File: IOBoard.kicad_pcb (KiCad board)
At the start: 2 copper layers, 119.8 x 63.7 mm, 29 parts, among them J12 DE9_Receptacle, J13 DE9_Plug, J14 DE9_Receptacle, J15 DE9_Receptacle, J16 DE9_Receptacle, J3 Conn_01x03, J4 Conn_01x03, J5 Conn_01x03, J6 Conn_01x03, J7 Conn_01x03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

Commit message: Update schematic and PCB to use resistor symbols instead of jumpers.
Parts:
- removed JP1, JP10, JP11, JP12, JP13, JP14, JP15, JP16, JP2, JP3, JP4, JP5, JP6, JP7, JP8, JP9: Jumper_2_Open, Resistor_THT:R_Axial_DIN0207_L6.3mm_D2.5mm_P10.16mm_Horizontal
- added R10: 120R, Resistor_THT:R_Axial_DIN0207_L6.3mm_D2.5mm_P7.62mm_Horizontal, F.Cu at (156.2, 121.9)
- added R11: 120R, Resistor_THT:R_Axial_DIN0207_L6.3mm_D2.5mm_P7.62mm_Horizontal, F.Cu at (156.2, 118.1)
- added R12: 120R, Resistor_THT:R_Axial_DIN0207_L6.3mm_D2.5mm_P7.62mm_Horizontal, F.Cu at (156.2, 114.3)
- added R13: 120R, Resistor_THT:R_Axial_DIN0207_L6.3mm_D2.5mm_P7.62mm_Horizontal, F.Cu at (156.2, 110.5)
- added R14: 120R, Resistor_THT:R_Axial_DIN0207_L6.3mm_D2.5mm_P7.62mm_Horizontal, F.Cu at (156.2, 106.7)
- added R15: 120R, Resistor_THT:R_Axial_DIN0207_L6.3mm_D2.5mm_P7.62mm_Horizontal, F.Cu at (156.2, 102.9)
- added R16: 120R, Resistor_THT:R_Axial_DIN0207_L6.3mm_D2.5mm_P7.62mm_Horizontal, F.Cu at (156.2, 99.1)
- added R17: 120R, Resistor_THT:R_Axial_DIN0207_L6.3mm_D2.5mm_P7.62mm_Horizontal, F.Cu at (156.2, 95.2)
- added R2: 120R, Resistor_THT:R_Axial_DIN0207_L6.3mm_D2.5mm_P7.62mm_Horizontal, F.Cu at (125.7, 95.2)
- added R3: 120R, Resistor_THT:R_Axial_DIN0207_L6.3mm_D2.5mm_P7.62mm_Horizontal, F.Cu at (125.7, 99.1)
- added R4: 120R, Resistor_THT:R_Axial_DIN0207_L6.3mm_D2.5mm_P7.62mm_Horizontal, F.Cu at (125.7, 102.9)
- added R5: 120R, Resistor_THT:R_Axial_DIN0207_L6.3mm_D2.5mm_P7.62mm_Horizontal, F.Cu at (125.7, 106.7)
- added R6: 120R, Resistor_THT:R_Axial_DIN0207_L6.3mm_D2.5mm_P7.62mm_Horizontal, F.Cu at (125.7, 110.5)
- added R7: 120R, Resistor_THT:R_Axial_DIN0207_L6.3mm_D2.5mm_P7.62mm_Horizontal, F.Cu at (125.7, 114.3)
- added R8: 120R, Resistor_THT:R_Axial_DIN0207_L6.3mm_D2.5mm_P7.62mm_Horizontal, F.Cu at (125.7, 118.1)
- added R9: 120R, Resistor_THT:R_Axial_DIN0207_L6.3mm_D2.5mm_P7.62mm_Horizontal, F.Cu at (125.7, 121.9)
- moved J16 2.54 mm to (166.4, 113.0)
- moved J15 1.69 mm to (114.4, 102.1)
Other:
- board size 119.8 x 63.7 mm -> 118.5 x 63.7 mm

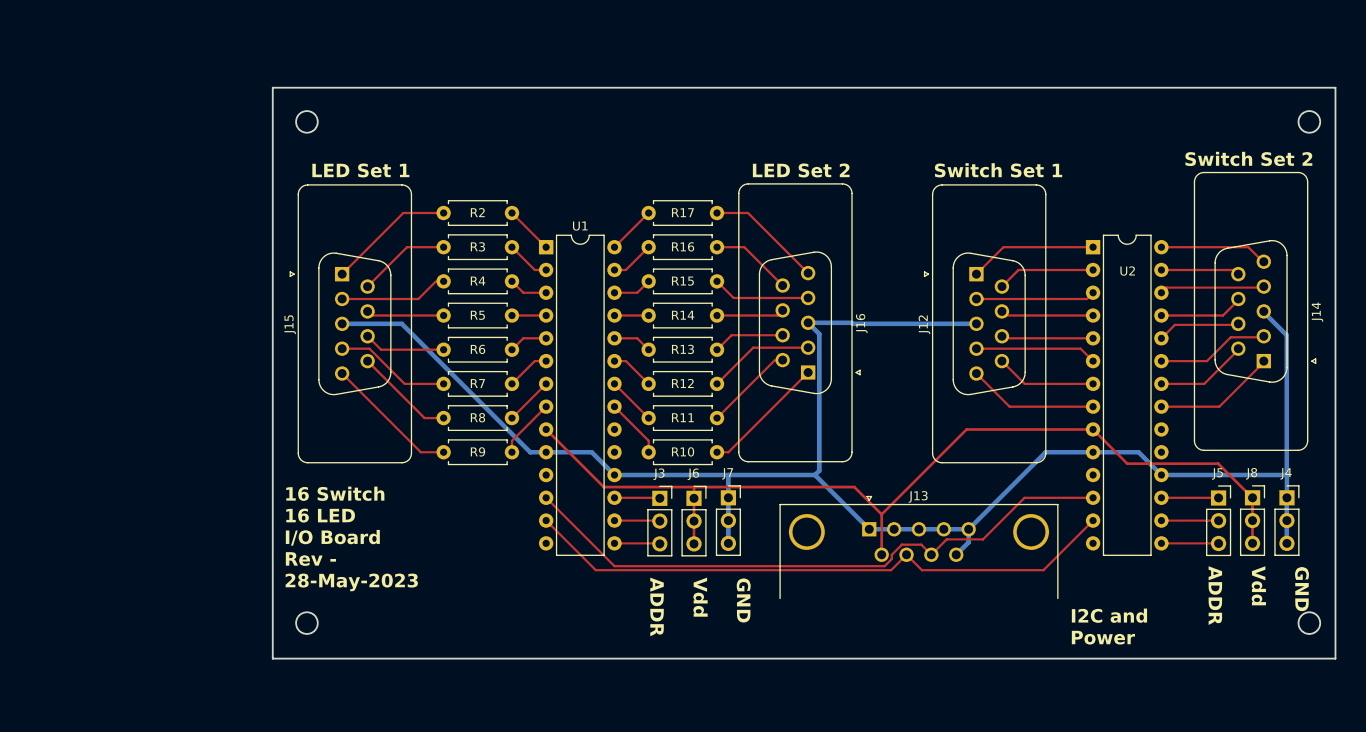
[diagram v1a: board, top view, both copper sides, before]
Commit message: Update PCB to use SMD resistors and rectangular connectors.  This lets the PCB shrink some more and it may be easier to crimp rectangular connectors onto ribbon cable than to solder a bunch of D-9 connectors.
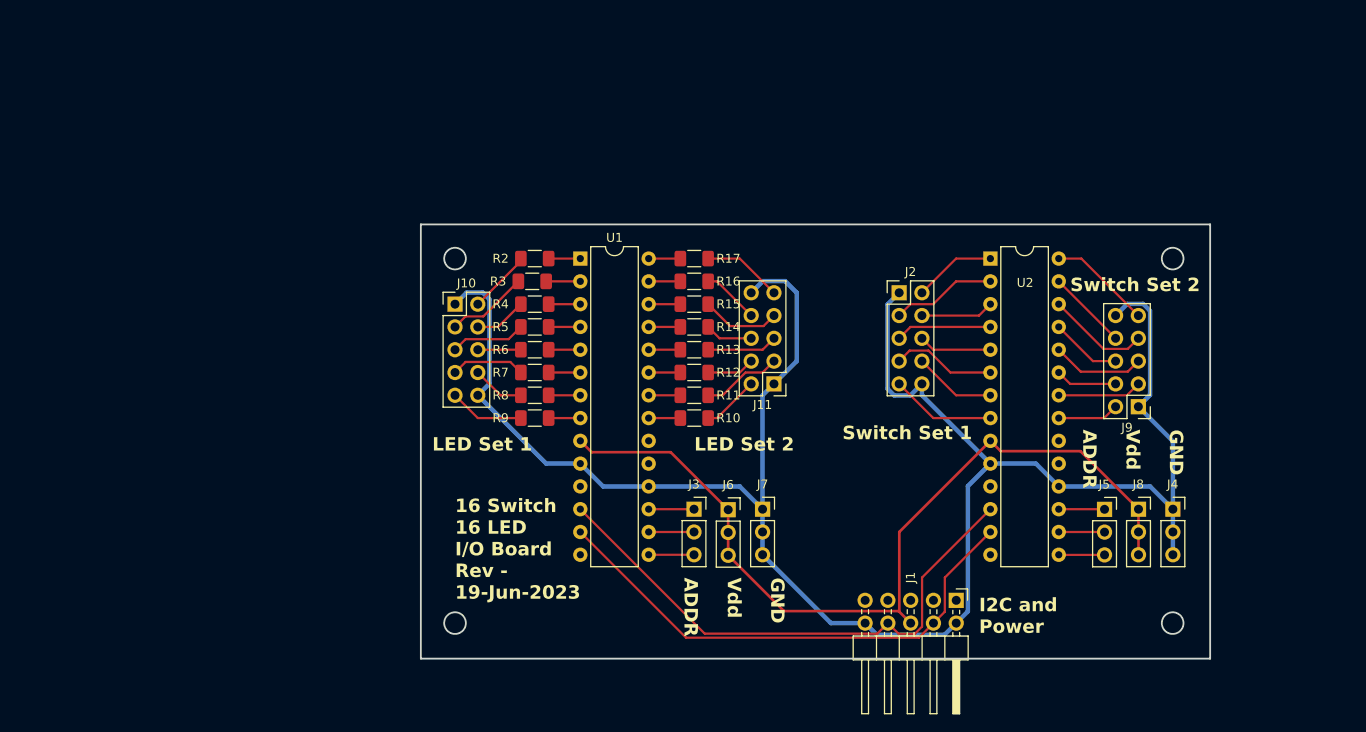
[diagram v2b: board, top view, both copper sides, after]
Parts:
- removed J12, J14, J15, J16: DE9_Receptacle, Connector_Dsub:DSUB-9_Female_Vertical_P2.77x2.84mm
- removed J13: DE9_Plug, Connector_Dsub:DSUB-9_Male_Horizontal_P2.77x2.84mm_EdgePinOffset4.94mm_Housed_MountingHolesOffset7.48mm
- added J1: Conn_02x05_Odd_Even, Connector_PinHeader_2.54mm:PinHeader_2x05_P2.54mm_Horizontal, F.Cu at (182.9, 138.4)
- added J10: Conn_02x05_Odd_Even, Connector_PinHeader_2.54mm:PinHeader_2x05_P2.54mm_Vertical, F.Cu at (127.0, 105.4)
- added J11: Conn_02x05_Odd_Even, Connector_PinHeader_2.54mm:PinHeader_2x05_P2.54mm_Vertical, F.Cu at (162.6, 114.3)
- added J2: Conn_02x05_Odd_Even, Connector_PinHeader_2.54mm:PinHeader_2x05_P2.54mm_Vertical, F.Cu at (176.5, 104.1)
- added J9: Conn_02x05_Odd_Even, Connector_PinHeader_2.54mm:PinHeader_2x05_P2.54mm_Vertical, F.Cu at (203.2, 116.8)
- R10, R11, R12, R13, R14, R15, R16, R17, R2, R3, R4, R5, R6, R7, R8, R9: footprint Resistor_THT:R_Axial_DIN0207_L6.3mm_D2.5mm_P7.62mm_Horizontal -> Resistor_SMD:R_1206_3216Metric_Pad1.30x1.75mm_HandSolder
- moved J4 12.8 mm to (207.0, 128.3)
- moved J8 12.8 mm to (203.2, 128.3)
- moved J5 12.8 mm to (199.4, 128.3)
- moved U2 11.5 mm to (186.7, 100.3)
- moved R2 11.4 mm to (135.9, 100.3)
- moved R9 10.9 mm to (135.9, 118.1)
- moved R3 10.6 mm to (135.6, 102.9)
- moved R8 10.5 mm to (135.9, 115.6)
- moved R4 10.5 mm to (135.9, 105.4)
- moved R5 10.2 mm to (135.9, 108.0)
- moved R7 10.2 mm to (135.9, 113.0)
- moved R6 10.2 mm to (135.9, 110.5)
- moved R17 5.68 mm to (153.7, 100.3)
- moved R10 4.58 mm to (153.7, 118.1)
- moved R16 4.58 mm to (153.7, 102.9)
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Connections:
- net Net-(U1-SCK) renamed /SCK
- net Net-(U1-SDA) renamed /SDA
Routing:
- net GND: track 193.8 -> 219.5 mm
- net +3.3V: track 105.7 -> 96.2 mm
- net /SDA: track 67.0 -> 57.7 mm
- net Net-(J11-Pin_2): track 13.8 -> 6.38 mm
- net /SCK: track 68.5 -> 61.4 mm
- net Net-(J9-Pin_2): track 13.5 -> 6.86 mm
- net Net-(J11-Pin_4): track 11.8 -> 5.33 mm
- net Net-(J10-Pin_2): track 13.3 -> 7.07 mm
- net Net-(J10-Pin_9): track 14.1 -> 8.39 mm
- net Net-(J9-Pin_4): track 12.5 -> 6.86 mm
- net Net-(J10-Pin_4): track 11.3 -> 5.85 mm
- net Net-(J2-Pin_4): track 13.3 -> 8.16 mm
- net Net-(J2-Pin_2): track 14.2 -> 9.21 mm
- net Net-(J10-Pin_8): track 10.3 -> 5.85 mm
- net Net-(J11-Pin_9): track 12.9 -> 8.92 mm
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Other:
- board size 118.5 x 63.7 mm -> 88 x 48.4 mm
- board text added: "16 Switch 16 LED I/O Board Rev - 19-Jun-2023"
- board text removed: "16 Switch 16 LED I/O Board Rev - 28-May-2023"

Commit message: Update schematic to add resisters on inputs as well.  Submitted PCB for production.  Once PCBs are received, assembled, tested, and working, I'll update documentation.
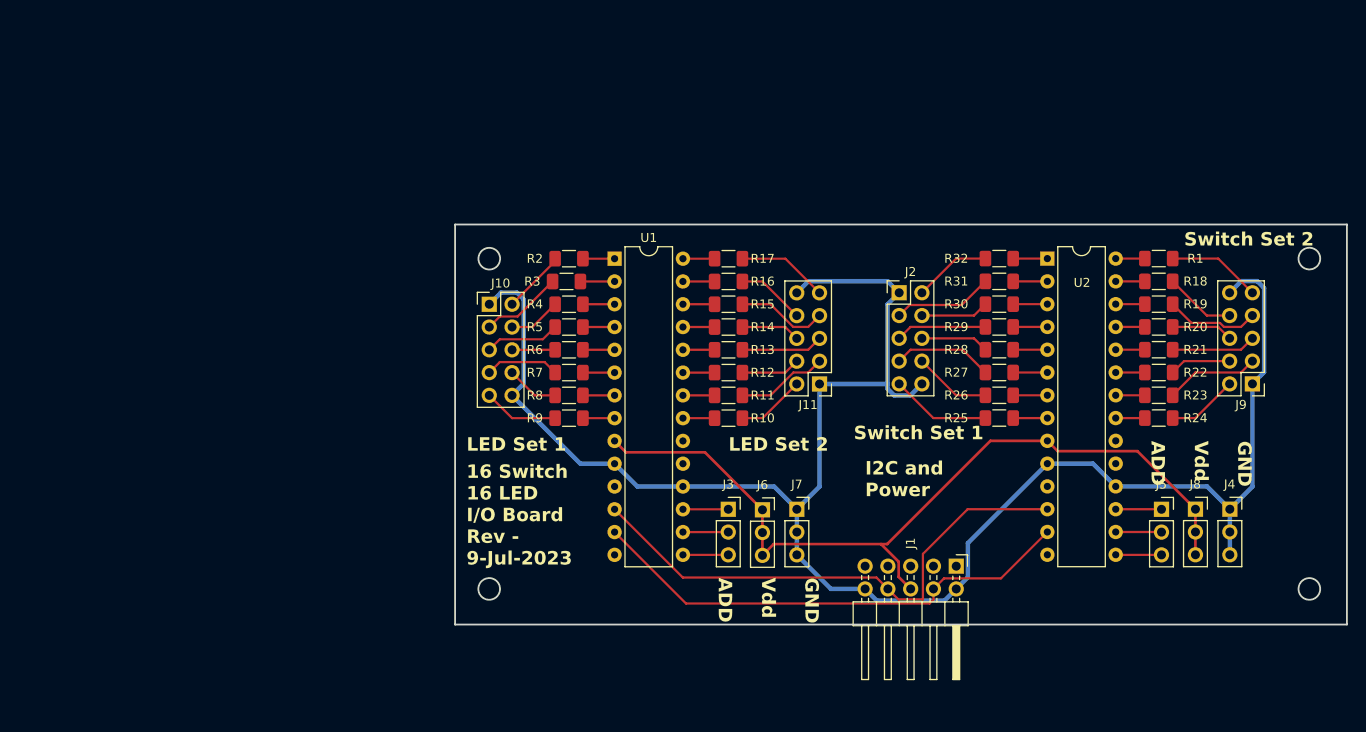
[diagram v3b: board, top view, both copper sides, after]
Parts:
- added R1: 1k, Resistor_SMD:R_1206_3216Metric_Pad1.30x1.75mm_HandSolder, F.Cu at (205.5, 100.3)
- added R18: 1k, Resistor_SMD:R_1206_3216Metric_Pad1.30x1.75mm_HandSolder, F.Cu at (205.5, 102.9)
- added R19: 1k, Resistor_SMD:R_1206_3216Metric_Pad1.30x1.75mm_HandSolder, F.Cu at (205.5, 105.4)
- added R20: 1k, Resistor_SMD:R_1206_3216Metric_Pad1.30x1.75mm_HandSolder, F.Cu at (205.5, 108.0)
- added R21: 1k, Resistor_SMD:R_1206_3216Metric_Pad1.30x1.75mm_HandSolder, F.Cu at (205.5, 110.5)
- added R22: 1k, Resistor_SMD:R_1206_3216Metric_Pad1.30x1.75mm_HandSolder, F.Cu at (205.5, 113.0)
- added R23: 1k, Resistor_SMD:R_1206_3216Metric_Pad1.30x1.75mm_HandSolder, F.Cu at (205.5, 115.6)
- added R24: 1k, Resistor_SMD:R_1206_3216Metric_Pad1.30x1.75mm_HandSolder, F.Cu at (205.5, 118.1)
- added R25: 1k, Resistor_SMD:R_1206_3216Metric_Pad1.30x1.75mm_HandSolder, F.Cu at (187.7, 118.1)
- added R26: 1k, Resistor_SMD:R_1206_3216Metric_Pad1.30x1.75mm_HandSolder, F.Cu at (187.7, 115.6)
- added R27: 1k, Resistor_SMD:R_1206_3216Metric_Pad1.30x1.75mm_HandSolder, F.Cu at (187.7, 113.0)
- added R28: 1k, Resistor_SMD:R_1206_3216Metric_Pad1.30x1.75mm_HandSolder, F.Cu at (187.7, 110.5)
- added R29: 1k, Resistor_SMD:R_1206_3216Metric_Pad1.30x1.75mm_HandSolder, F.Cu at (187.7, 108.0)
- added R30: 1k, Resistor_SMD:R_1206_3216Metric_Pad1.30x1.75mm_HandSolder, F.Cu at (187.7, 105.4)
- added R31: 1k, Resistor_SMD:R_1206_3216Metric_Pad1.30x1.75mm_HandSolder, F.Cu at (187.7, 102.9)
- added R32: 1k, Resistor_SMD:R_1206_3216Metric_Pad1.30x1.75mm_HandSolder, F.Cu at (187.7, 100.3)
- moved J9 13.0 mm to (215.9, 114.3)
- moved J8 6.35 mm to (209.6, 128.3)
- moved J4 6.35 mm to (213.4, 128.3)
- moved J5 6.35 mm to (205.8, 128.3)
- moved U2 6.35 mm to (193.0, 100.3)
- moved J11 5.08 mm to (167.6, 114.3)
- moved J7 3.82 mm to (165.1, 128.3)
- moved R10 3.82 mm to (157.5, 118.1)
- moved R11 3.82 mm to (157.5, 115.6)
- moved R12 3.82 mm to (157.5, 113.0)
- moved R13 3.82 mm to (157.5, 110.5)
- moved R14 3.82 mm to (157.5, 108.0)
- moved R15 3.82 mm to (157.5, 105.4)
- moved R16 3.82 mm to (157.5, 102.9)
- moved R17 3.82 mm to (157.5, 100.3)
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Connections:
- U2 pad 1: Net-(J2-Pin_2) -> Net-(U2-GPB0)
- U2 pad 2: Net-(J2-Pin_3) -> Net-(U2-GPB1)
- U2 pad 21: Net-(J9-Pin_2) -> Net-(U2-GPA0)
- U2 pad 22: Net-(J9-Pin_3) -> Net-(U2-GPA1)
- U2 pad 23: Net-(J9-Pin_4) -> Net-(U2-GPA2)
- U2 pad 24: Net-(J9-Pin_5) -> Net-(U2-GPA3)
- U2 pad 25: Net-(J9-Pin_6) -> Net-(U2-GPA4)
- U2 pad 26: Net-(J9-Pin_7) -> Net-(U2-GPA5)
- U2 pad 27: Net-(J9-Pin_8) -> Net-(U2-GPA6)
- U2 pad 28: Net-(J9-Pin_9) -> Net-(U2-GPA7)
- U2 pad 3: Net-(J2-Pin_4) -> Net-(U2-GPB2)
- U2 pad 4: Net-(J2-Pin_5) -> Net-(U2-GPB3)
- U2 pad 5: Net-(J2-Pin_6) -> Net-(U2-GPB4)
- U2 pad 6: Net-(J2-Pin_7) -> Net-(U2-GPB5)
- U2 pad 7: Net-(J2-Pin_8) -> Net-(U2-GPB6)
- U2 pad 8: Net-(J2-Pin_9) -> Net-(U2-GPB7)
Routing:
- net GND: track 219.5 -> 206.1 mm
- net Net-(U2-GPB7): track 0.00 -> 3.81 mm
- net Net-(U2-GPB6): track 0.00 -> 3.81 mm
- net Net-(U2-GPB5): track 0.00 -> 3.81 mm
- net Net-(U2-GPB4): track 0.00 -> 3.81 mm
- net Net-(U2-GPB3): track 0.00 -> 3.81 mm
- net Net-(U2-GPB2): track 0.00 -> 3.81 mm
- net Net-(U2-GPB1): track 0.00 -> 3.81 mm
- net Net-(U2-GPB0): track 0.00 -> 3.81 mm
- net +3.3V: track 96.2 -> 92.9 mm
- net Net-(U2-GPA7): track 0.00 -> 3.25 mm
- net Net-(U2-GPA6): track 0.00 -> 3.25 mm
- net Net-(U2-GPA5): track 0.00 -> 3.25 mm
- net Net-(U2-GPA4): track 0.00 -> 3.25 mm
- net Net-(U2-GPA3): track 0.00 -> 3.25 mm
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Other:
- board size 88 x 48.4 mm -> 99.4 x 44.6 mm
- board text added: "16 Switch 16 LED I/O Board Rev - 9-Jul-2023"
- board text added: "GND Vdd ADD"
- board text removed: "16 Switch 16 LED I/O Board Rev - 19-Jun-2023"
- board text removed: "GND Vdd ADDR"

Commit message: Fix schematic error and re-layout board.  Start a tray to hold board.
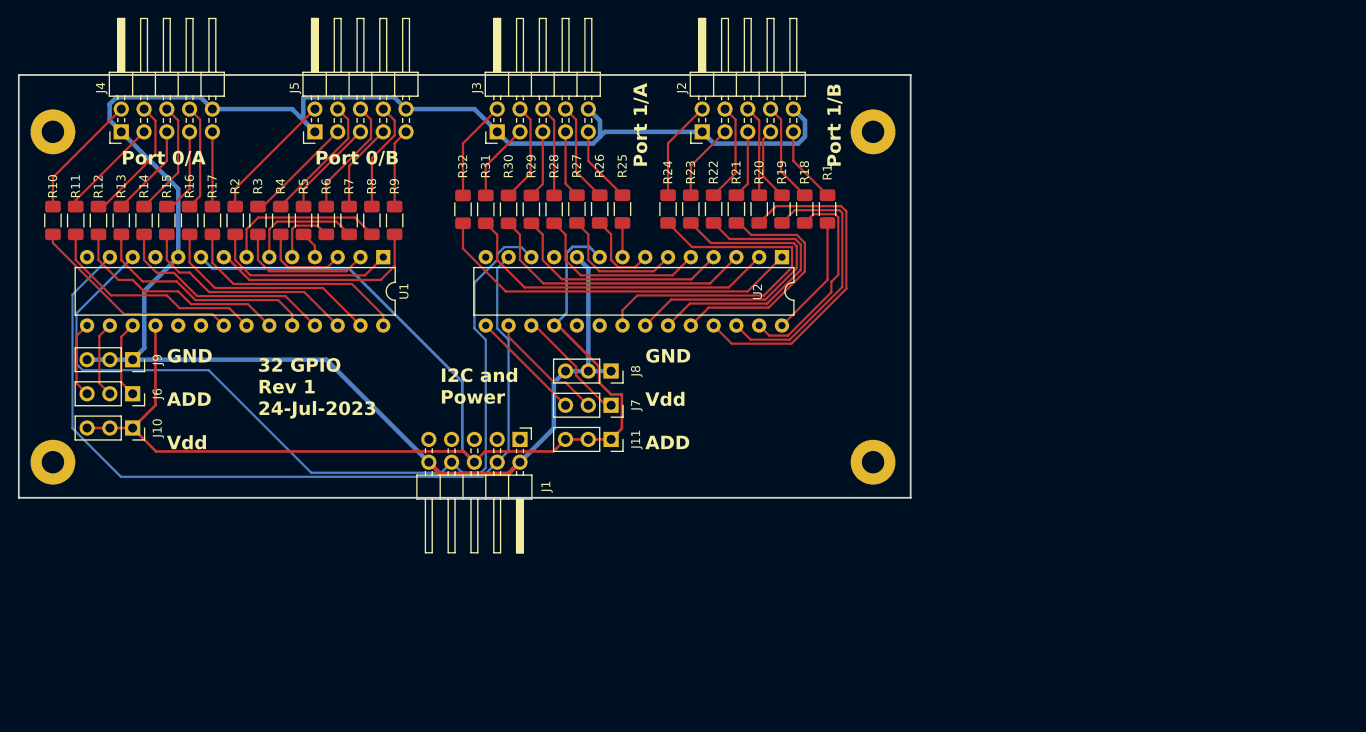
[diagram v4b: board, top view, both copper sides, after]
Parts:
- added H1: MountingHole_2.5mm_Pad, MountingHole:MountingHole_2.5mm_Pad, F.Cu at (82.2, 86.2)
- added H2: MountingHole_2.5mm_Pad, MountingHole:MountingHole_2.5mm_Pad, F.Cu at (173.6, 86.2)
- added H3: MountingHole_2.5mm_Pad, MountingHole:MountingHole_2.5mm_Pad, F.Cu at (82.2, 123.0)
- added H4: MountingHole_2.5mm_Pad, MountingHole:MountingHole_2.5mm_Pad, F.Cu at (173.6, 123.0)
- J2: renamed from J9; footprint Connector_PinHeader_2.54mm:PinHeader_2x05_P2.54mm_Vertical -> Connector_PinHeader_2.54mm:PinHeader_2x05_P2.54mm_Horizontal
- J3: renamed from J2; footprint Connector_PinHeader_2.54mm:PinHeader_2x05_P2.54mm_Vertical -> Connector_PinHeader_2.54mm:PinHeader_2x05_P2.54mm_Horizontal
- J4: renamed from J11; footprint Connector_PinHeader_2.54mm:PinHeader_2x05_P2.54mm_Vertical -> Connector_PinHeader_2.54mm:PinHeader_2x05_P2.54mm_Horizontal
- J5: renamed from J10; footprint Connector_PinHeader_2.54mm:PinHeader_2x05_P2.54mm_Vertical -> Connector_PinHeader_2.54mm:PinHeader_2x05_P2.54mm_Horizontal
- moved J4 82.8 mm to (89.8, 86.2), turned to 90 degrees
- moved R10 78.5 mm to (82.2, 96.1), turned to -90 degrees
- moved J9 75.9 mm to (91.1, 111.6), turned to -90 degrees
- moved R11 75.3 mm to (84.7, 96.1), turned to -90 degrees
- moved R12 72.3 mm to (87.2, 96.1), turned to -90 degrees
- moved J10 70.8 mm to (91.1, 119.2), turned to -90 degrees
- moved J8 70.7 mm to (144.4, 112.9), turned to -90 degrees
- moved R13 69.2 mm to (89.8, 96.1), turned to -90 degrees
- moved J6 67.6 mm to (91.1, 115.4), turned to -90 degrees
- moved J2 67.5 mm to (154.6, 86.2), turned to 90 degrees
- moved R14 66.2 mm to (92.3, 96.1), turned to -90 degrees
- moved J11 65.6 mm to (144.4, 120.5), turned to -90 degrees
- moved R15 63.3 mm to (94.9, 96.1), turned to -90 degrees
- moved J7 62.5 mm to (144.4, 116.7), turned to -90 degrees
- moved R16 60.5 mm to (97.4, 96.1), turned to -90 degrees
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- renumbered J6 to J10, J8 to J11, J3 to J6, J5 to J7, J4 to J8, J7 to J9
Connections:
- U1 pad 18: GND -> +3.3V
- U2 pad 18: GND -> +3.3V
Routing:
- net +3.3V: track 92.9 -> 148.3 mm
- net /SDA: track 55.6 -> 95.5 mm
- net Net-(U2-GPB0): track 3.81 -> 42.0 mm
- net /SCK: track 59.6 -> 96.4 mm
- net Net-(U2-GPA0): track 3.25 -> 39.8 mm
- net Net-(U2-GPA4): track 3.25 -> 37.5 mm
- net Net-(U2-GPB1): track 3.81 -> 36.5 mm
- net Net-(U2-GPA1): track 3.25 -> 34.9 mm
- net Net-(U2-GPA2): track 3.25 -> 30.9 mm
- net Net-(U2-GPA5): track 3.25 -> 30.6 mm
- net Net-(U2-GPB2): track 3.81 -> 31.0 mm
- net Net-(U2-GPA3): track 3.25 -> 27.0 mm
- net Net-(U1-GPA7): track 3.53 -> 25.8 mm
- net Net-(U1-GPA3): track 3.53 -> 25.7 mm
- net Net-(U2-GPB3): track 3.81 -> 25.6 mm
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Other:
- board size 99.4 x 44.6 mm -> 99.4 x 47.1 mm
- board text added: "32 GPIO Rev 1 24-Jul-2023"
- board text added: "GND ADD Vdd"
- board text added: "Port 0/A"
- board text added: "Port 0/B"
- board text added: "Port 1/A"
- board text added: "Port 1/B"
- board text removed: "16 Switch 16 LED I/O Board Rev - 9-Jul-2023"
- board text removed: "LED Set 1"
- board text removed: "LED Set 2"
- board text removed: "Switch Set 1"
- board text removed: "Switch Set 2"
